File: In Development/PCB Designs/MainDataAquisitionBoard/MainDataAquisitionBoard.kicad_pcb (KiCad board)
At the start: 2 copper layers, 26 parts, among them J1 Motor Driver, J10 3V3, J11 GND, J12 Hall Effect, J13 Hall Effect 2, J14 12V In, J15 Conn_01x08, J16 MotorDriver2, J17 GND In, J2 Conn_01x01, J3 Conn_01x01, J4 1x24, J5 Teensy 3.6L, J6 Teensy 3.6R, J7 1x24, J8 5V, J9 LDS, U1 L7805

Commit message: Finished main DAQ PCB
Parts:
- removed J15: Conn_01x08, Connector_PinHeader_2.54mm:PinHeader_1x08_P2.54mm_Vertical
- removed J16: MotorDriver2, Connector_PinHeader_2.54mm:PinHeader_1x02_P2.54mm_Vertical
- removed J17: GND In, Connector_PinHeader_2.54mm:PinHeader_1x01_P2.54mm_Vertical
- removed U1: L7805, Package_TO_SOT_THT:TO-220-3_Horizontal_TabDown
- J1: value Motor Driver -> Conn_01x08; footprint Connector_PinHeader_2.54mm:PinHeader_1x08_P2.54mm_Vertical -> Connector_PinHeader_2.00mm:PinHeader_1x08_P2.00mm_Vertical
- J10: value 3V3 -> 3v3; footprint Connector_PinHeader_2.54mm:PinHeader_1x05_P2.54mm_Vertical -> Connector_PinHeader_2.54mm:PinHeader_1x04_P2.54mm_Vertical
- J11: value GND -> TopR; footprint Connector_PinHeader_2.54mm:PinHeader_1x05_P2.54mm_Vertical -> CustomKiCADLibrary:PinHeader_1x10_P5.08mm_Vertical
- J12: value Hall Effect -> TopL; footprint Connector_PinHeader_2.54mm:PinHeader_1x04_P2.54mm_Vertical -> CustomKiCADLibrary:PinHeader_1x10_P5.08mm_Vertical
- J13: value Hall Effect 2 -> BottomR; footprint Connector_PinHeader_2.54mm:PinHeader_1x04_P2.54mm_Vertical -> CustomKiCADLibrary:PinHeader_1x10_P5.08mm_Vertical
- J14: value 12V In -> BottomL; footprint Connector_PinHeader_2.54mm:PinHeader_1x01_P2.54mm_Vertical -> CustomKiCADLibrary:PinHeader_1x10_P5.08mm_Vertical
- J2: value Conn_01x01 -> Conn_01x08; footprint Connector_PinHeader_2.54mm:PinHeader_1x01_P2.54mm_Vertical -> Connector_PinHeader_2.00mm:PinHeader_1x08_P2.00mm_Vertical
- J3: value Conn_01x01 -> GND; footprint Connector_PinHeader_2.54mm:PinHeader_1x01_P2.54mm_Vertical -> Connector_PinHeader_2.54mm:PinHeader_1x04_P2.54mm_Vertical
- J8: footprint Connector_PinHeader_2.54mm:PinHeader_1x05_P2.54mm_Vertical -> Connector_PinHeader_2.54mm:PinHeader_1x04_P2.54mm_Vertical
- J9: value LDS -> Conn_01x04; footprint Connector_PinHeader_2.54mm:PinHeader_1x03_P2.54mm_Vertical -> Connector_PinHeader_2.54mm:PinHeader_1x04_P2.54mm_Vertical
- R1, R3, R5, R7: value 5.1k -> 4.7k
- moved J2 139.2 mm to (72.4, 130.8), turned to 180 degrees
- moved J9 108.2 mm to (172.7, 83.8), turned to 90 degrees
- moved R8 102.9 mm to (180.3, 111.8), turned to 90 degrees
- moved J1 100.7 mm to (72.4, 95.2), turned to 180 degrees
- moved R7 100.6 mm to (180.3, 99.1), turned to 90 degrees
- moved R6 99.6 mm to (175.3, 111.8), turned to 90 degrees
- moved R5 96.7 mm to (175.3, 99.1), turned to 90 degrees
- moved J11 88.0 mm to (81.3, 69.8)
- moved J14 80.8 mm to (135.9, 66.0), turned to 90 degrees
- moved J12 70.0 mm to (133.3, 69.8), turned to 90 degrees
- moved J3 56.1 mm to (153.7, 123.2)
- moved J10 27.2 mm to (143.5, 123.2), turned to 0 degrees
- moved J8 27.2 mm to (148.6, 123.2), turned to 0 degrees
- moved J13 20.5 mm to (83.8, 66.0), turned to 90 degrees
- moved R2 19.2 mm to (78.7, 110.5), turned to 90 degrees
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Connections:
- J1 pad 1: Net-(J1-Pad1) -> (no net)
- J1 pad 2: Net-(J1-Pad2) -> (no net)
- J1 pad 5: Net-(J1-Pad5) -> (no net)
- J1 pad 6: Net-(J1-Pad6) -> (no net)
- J1 pad 7: Net-(J1-Pad7) -> (no net)
- J11 pad 1: Net-(J1-Pad1) -> Net-(J11-Pad1)
- J11 pad 2: Net-(J1-Pad1) -> Net-(J11-Pad2)
- J11 pad 3: Net-(J1-Pad1) -> Net-(J11-Pad2)
- J11 pad 4: Net-(J1-Pad1) -> Net-(J11-Pad2)
- J11 pad 5: Net-(J1-Pad1) -> Net-(J11-Pad2)
- J12 pad 2: Net-(J1-Pad1) -> Net-(J10-Pad1)
- J12 pad 3: Net-(J12-Pad3) -> Net-(J10-Pad1)
- J13 pad 1: Net-(J12-Pad1) -> Net-(J13-Pad1)
- J13 pad 2: Net-(J1-Pad1) -> Net-(J13-Pad10)
- J13 pad 3: Net-(J13-Pad3) -> Net-(J13-Pad10)
- J13 pad 4: Net-(J13-Pad4) -> Net-(J13-Pad10)
- J2 pad 1: (no net) -> Net-(J11-Pad2)
- J3 pad 1: (no net) -> Net-(J13-Pad10)
- J4 pad 1: Net-(J1-Pad1) -> Net-(J13-Pad10)
- J4 pad 4: Net-(J1-Pad2) -> Net-(J4-Pad4)
- J4 pad 5: Net-(J1-Pad3) -> Net-(J4-Pad5)
- J4 pad 7: Net-(J4-Pad7) -> Net-(J2-Pad8)
- J4 pad 8: Net-(J4-Pad8) -> Net-(J2-Pad4)
- J5 pad 1: Net-(J1-Pad1) -> Net-(J13-Pad10)
- J5 pad 4: Net-(J1-Pad2) -> Net-(J4-Pad4)
- J5 pad 5: Net-(J1-Pad3) -> Net-(J4-Pad5)
- J5 pad 7: Net-(J4-Pad7) -> Net-(J2-Pad8)
- J5 pad 8: Net-(J4-Pad8) -> Net-(J2-Pad4)
- J6 pad 1: Net-(J12-Pad1) -> Net-(J11-Pad2)
- J6 pad 10: Net-(J6-Pad10) -> Net-(J14-Pad4)
- J6 pad 11: Net-(J13-Pad3) -> Net-(J12-Pad4)
- J6 pad 12: Net-(J13-Pad4) -> Net-(J14-Pad7)
- J6 pad 13: Net-(J6-Pad13) -> Net-(J12-Pad7)
- J6 pad 24: Net-(J6-Pad24) -> Net-(J1-Pad8)
- J6 pad 4: Net-(J6-Pad4) -> Net-(J13-Pad8)
- J6 pad 5: Net-(J6-Pad5) -> Net-(J11-Pad8)
- J6 pad 6: Net-(J6-Pad6) -> Net-(J14-Pad1)
- J6 pad 7: Net-(J12-Pad3) -> Net-(J12-Pad1)
- J6 pad 8: Net-(J12-Pad4) -> Net-(J11-Pad1)
- J6 pad 9: Net-(J6-Pad9) -> Net-(J13-Pad1)
- J7 pad 1: Net-(J12-Pad1) -> Net-(J11-Pad2)
- J7 pad 10: Net-(J6-Pad10) -> Net-(J14-Pad4)
- J7 pad 11: Net-(J13-Pad3) -> Net-(J12-Pad4)
- J7 pad 12: Net-(J13-Pad4) -> Net-(J14-Pad7)
- J7 pad 13: Net-(J6-Pad13) -> Net-(J12-Pad7)
- J7 pad 24: Net-(J6-Pad24) -> Net-(J1-Pad8)
- J7 pad 4: Net-(J6-Pad4) -> Net-(J13-Pad8)
- J7 pad 5: Net-(J6-Pad5) -> Net-(J11-Pad8)
- J7 pad 6: Net-(J6-Pad6) -> Net-(J14-Pad1)
- J7 pad 7: Net-(J12-Pad3) -> Net-(J12-Pad1)
- J7 pad 8: Net-(J12-Pad4) -> Net-(J11-Pad1)
- J7 pad 9: Net-(J6-Pad9) -> Net-(J13-Pad1)
- J8 pad 1: Net-(J12-Pad1) -> Net-(J11-Pad2)
- J8 pad 2: Net-(J12-Pad1) -> Net-(J11-Pad2)
- J8 pad 3: Net-(J12-Pad1) -> Net-(J11-Pad2)
- J8 pad 4: Net-(J12-Pad1) -> Net-(J11-Pad2)
- J9 pad 1: Net-(J12-Pad1) -> Net-(J12-Pad9)
- J9 pad 2: Net-(J6-Pad13) -> Net-(J12-Pad10)
- J9 pad 3: Net-(J1-Pad1) -> Net-(J14-Pad9)
- R1 pad 1: Net-(J12-Pad3) -> Net-(J4-Pad24)
- R1 pad 2: Net-(J12-Pad1) -> Net-(J1-Pad3)
- R2 pad 1: Net-(J12-Pad3) -> Net-(J13-Pad10)
- R2 pad 2: Net-(J1-Pad1) -> Net-(J4-Pad24)
- R3 pad 1: Net-(J12-Pad4) -> Net-(J4-Pad23)
- R3 pad 2: Net-(J12-Pad1) -> Net-(J1-Pad4)
- R4 pad 1: Net-(J12-Pad4) -> Net-(J13-Pad10)
- R4 pad 2: Net-(J1-Pad1) -> Net-(J4-Pad23)
- R5 pad 1: Net-(J13-Pad3) -> Net-(J6-Pad22)
- R5 pad 2: Net-(J12-Pad1) -> Net-(J11-Pad6)
- R6 pad 1: Net-(J13-Pad3) -> Net-(J13-Pad10)
- R6 pad 2: Net-(J1-Pad1) -> Net-(J6-Pad22)
- R7 pad 1: Net-(J13-Pad4) -> Net-(J6-Pad21)
- R7 pad 2: Net-(J12-Pad1) -> Net-(J13-Pad6)
- R8 pad 1: Net-(J13-Pad4) -> Net-(J13-Pad10)
- R8 pad 2: Net-(J1-Pad1) -> Net-(J6-Pad21)
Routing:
- net Net-(J13-Pad10): track 0.00 -> 327.3 mm
- net Net-(J1-Pad1): track 259.8 -> 0.00 mm
- net Net-(J11-Pad2): track 0.00 -> 199.8 mm
- net Net-(J6-Pad21): track 5.08 -> 153.2 mm
- net Net-(J14-Pad7): track 0.00 -> 141.3 mm
- net Net-(J12-Pad1): track 188.9 -> 55.6 mm
- net Net-(J12-Pad7): track 0.00 -> 131.0 mm
- net Net-(J13-Pad1): track 0.00 -> 104.5 mm
- net Net-(J13-Pad6): track 0.00 -> 100.0 mm
- net Net-(J10-Pad1): track 89.7 -> 189.1 mm
- net Net-(J11-Pad1): track 0.00 -> 97.2 mm
- net Net-(J6-Pad22): track 5.08 -> 98.9 mm
- net Net-(J11-Pad6): track 0.00 -> 91.4 mm
- net Net-(J11-Pad8): track 0.00 -> 88.8 mm
- net Net-(J13-Pad8): track 0.00 -> 86.8 mm
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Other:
- board text removed: "3V3"
- board text removed: "5V"
- board text removed: "GND"
- board text removed: "VCC"

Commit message: Finished eCVT protoboard schematic
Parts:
- moved J3 7.62 mm to (161.3, 123.2)
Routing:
- net Net-(J13-Pad10): track 327.3 -> 338.1 mm
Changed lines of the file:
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@@
     (thickness 1.6)
     (drawings 7)
-    (tracks 320)
+    (tracks 323)
     (zones 0)
     (modules 22)
@@
   )
   (module Connector_PinHeader_2.54mm:PinHeader_1x04_P2.54mm_Vertical (layer F.Cu)
-    (at 153.67 123.19)
+    (at 161.29 123.19)
     (descr "Through hole straight pin header, 1x04, 2.54mm pitch, single row")
     (tags "Through hole pin header THT 1x04 2.54mm single row")
@@
   (segment (start 148.59 92.71) (end 148.59 97.79) (width 0.25) (layer F.Cu) (net 39) (status 30))
   (segment (start 148.59 91.61) (end 148.59 92.71) (width 0.25) (layer F.Cu) (net 39) (status 20))
-  (segment (start 153.67 130.81) (end 153.67 123.19) (width 0.25) (layer F.Cu) (net 39) (status 30))
-  (segment (start 153.67 123.19) (end 165.1 111.76) (width 0.25) (layer F.Cu) (net 39) (status 30))
   (segment (start 148.59 98.89) (end 148.59 97.79) (width 0.25) (layer F.Cu) (net 39) (status 20))
   (segment (start 161.46 111.76) (end 148.59 98.89) (width 0.25) (layer F.Cu) (net 39))
@@
   (segment (start 106.68 63.5) (end 111.76 63.5) (width 0.25) (layer F.Cu) (net 39))
   (segment (start 78.93 133.35) (end 72.39 126.81) (width 0.25) (layer F.Cu) (net 39))
-  (segment (start 153.67 130.81) (end 151.13 133.35) (width 0.25) (layer F.Cu) (net 39))
   (segment (start 151.13 133.35) (end 78.93 133.35) (width 0.25) (layer F.Cu) (net 39))
   (segment (start 78.74 120.46) (end 78.74 110.49) (width 0.25) (layer F.Cu) (net 39))
   (segment (start 72.39 126.81) (end 78.74 120.46) (width 0.25) (layer F.Cu) (net 39))
   (segment (start 78.74 110.49) (end 83.82 110.49) (width 0.25) (layer F.Cu) (net 39))
+  (segment (start 161.29 122.09) (end 161.29 123.19) (width 0.25) (layer F.Cu) (net 39))
+  (segment (start 171.62 111.76) (end 161.29 122.09) (width 0.25) (layer F.Cu) (net 39))
+  (segment (start 175.26 111.76) (end 171.62 111.76) (width 0.25) (layer F.Cu) (net 39))
+  (segment (start 161.29 123.19) (end 161.29 130.81) (width 0.25) (layer F.Cu) (net 39))
+  (segment (start 161.29 130.81) (end 158.75 133.35) (width 0.25) (layer F.Cu) (net 39))
+  (segment (start 158.75 133.35) (end 151.13 133.35) (width 0.25) (layer F.Cu) (net 39))
   (segment (start 130.81 92.71) (end 130.81 97.79) (width 0.25) (layer F.Cu) (net 40) (status 30))
   (segment (start 73.064999 124.135001) (end 76.524999 124.135001) (width 0.25) (layer B.Cu) (net 40))

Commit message: Finished Main DAQ PCB rev 2
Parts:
- removed R1, R3: 4.7k, Resistor_THT:R_Axial_DIN0207_L6.3mm_D2.5mm_P7.62mm_Horizontal
- removed R2, R4: 8.2k, Resistor_THT:R_Axial_DIN0207_L6.3mm_D2.5mm_P7.62mm_Horizontal
- added J15: RTC, Connector_PinHeader_2.54mm:PinHeader_1x08_P2.54mm_Vertical, F.Cu at (109.2, 113.0)
- moved J5 10.2 mm to (148.6, 87.6)
- moved J4 10.2 mm to (148.6, 82.5)
- moved J6 10.2 mm to (148.6, 102.9)
- moved J7 10.2 mm to (148.6, 108.0)
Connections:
- J4 pad 23: Net-(J4-Pad23) -> Net-(J1-Pad4)
- J4 pad 24: Net-(J4-Pad24) -> Net-(J1-Pad3)
- J5 pad 23: Net-(J4-Pad23) -> Net-(J1-Pad4)
- J5 pad 24: Net-(J4-Pad24) -> Net-(J1-Pad3)
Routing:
- net Net-(J10-Pad1): track 189.1 -> 248.9 mm
- net Net-(J6-Pad21): track 153.2 -> 187.2 mm
- net Net-(J13-Pad10): track 338.1 -> 369.4 mm
- net Net-(J11-Pad1): track 97.2 -> 125.5 mm
- net Net-(J11-Pad2): track 199.8 -> 226.1 mm
- net Net-(J4-Pad24): track 21.9 -> 0.00 mm
- net Net-(J13-Pad1): track 104.5 -> 125.4 mm
- net Net-(J4-Pad23): track 19.4 -> 0.00 mm
- net Net-(J1-Pad3): track 6.43 -> 24.4 mm
- net Net-(J1-Pad4): track 12.3 -> 28.2 mm
- net Net-(J14-Pad1): track 59.4 -> 49.3 mm
- net Net-(J13-Pad8): track 86.8 -> 76.7 mm
- net Net-(J12-Pad1): track 55.6 -> 45.5 mm
- net Net-(J11-Pad8): track 88.8 -> 78.6 mm
- net Net-(J14-Pad4): track 65.1 -> 54.9 mm
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
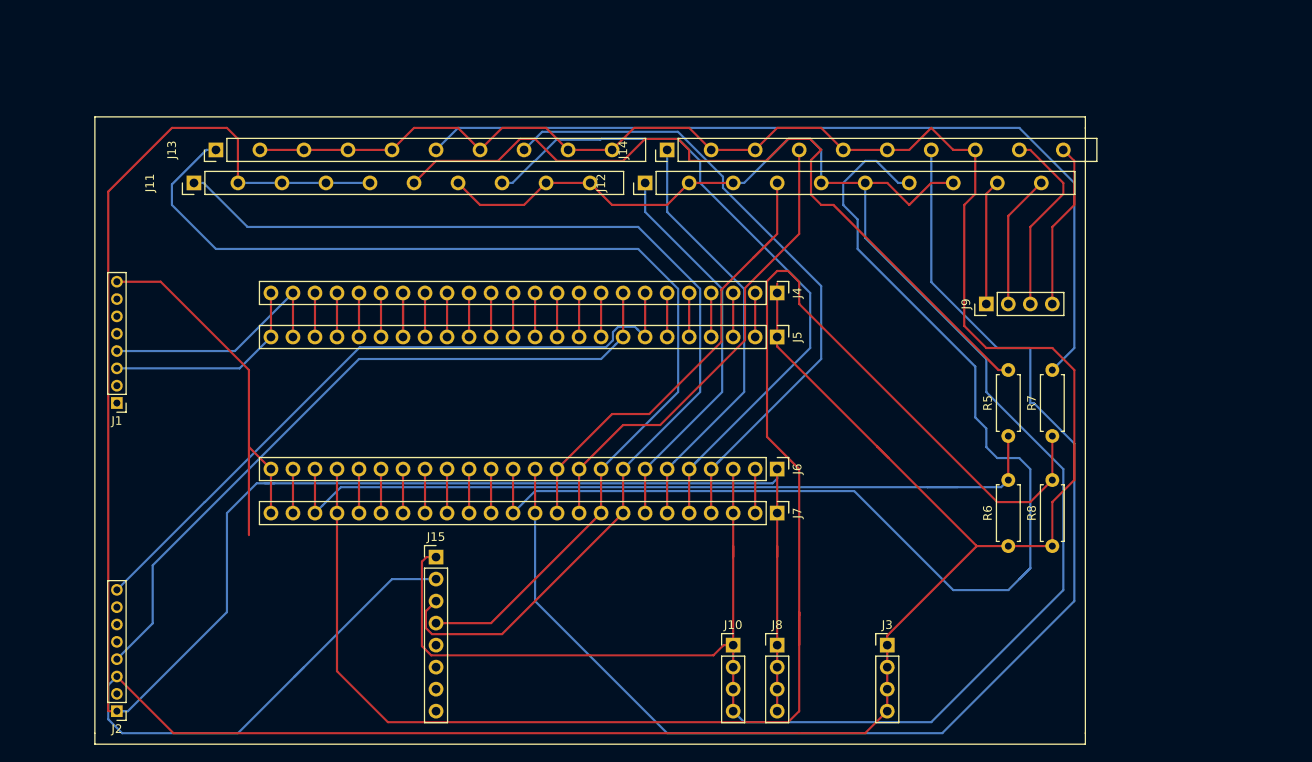
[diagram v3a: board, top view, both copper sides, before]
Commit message: Finished Main DAQ PCB and eCVT controller PCB for design review
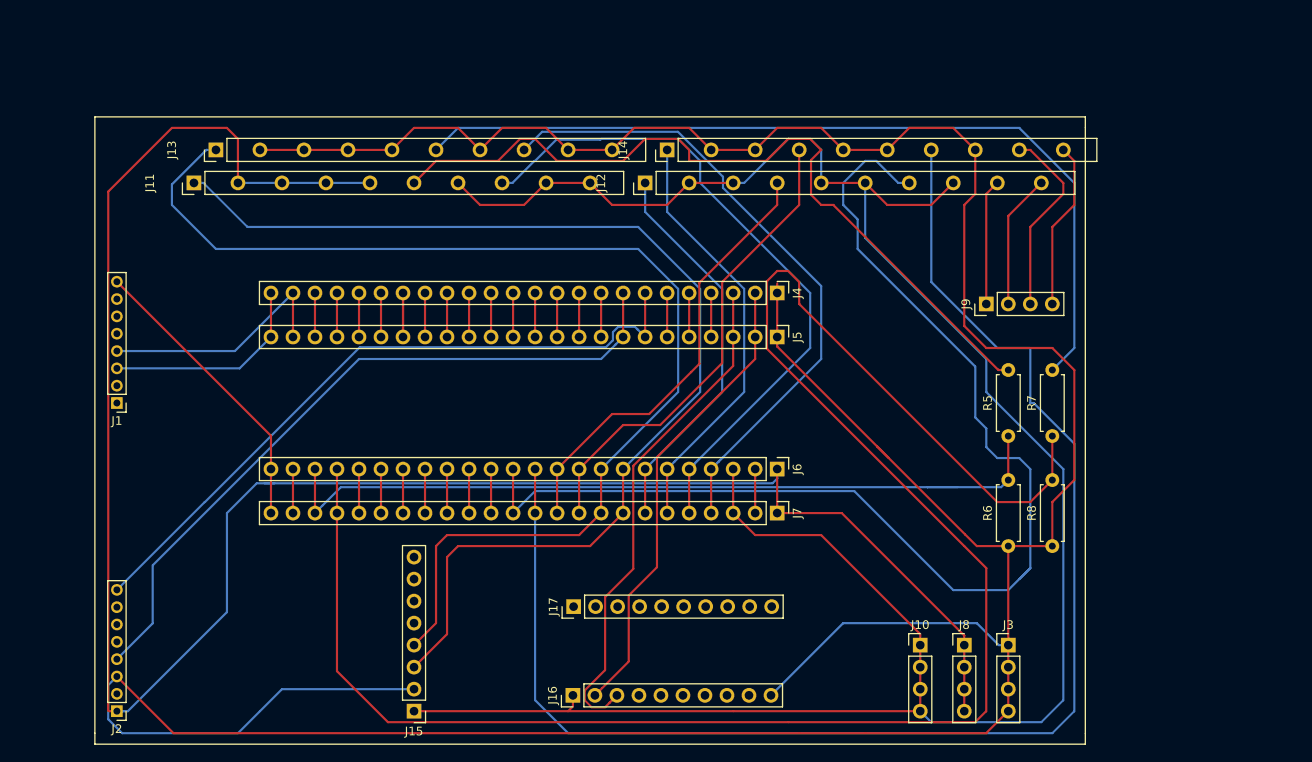
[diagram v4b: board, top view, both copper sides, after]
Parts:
- added J16: XbeeL, Connector_PinHeader_2.54mm:PinHeader_1x10_P2.54mm_Vertical, F.Cu at (125.0, 129.0)
- added J17: XbeeR, Connector_PinHeader_2.54mm:PinHeader_1x10_P2.54mm_Vertical, F.Cu at (125.1, 118.7)
- moved J10 21.6 mm to (165.1, 123.2)
- moved J8 21.6 mm to (170.2, 123.2)
- moved J15 18.0 mm to (106.7, 130.8), turned to 180 degrees
- moved J3 14.0 mm to (175.3, 123.2)
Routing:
- net Net-(J16-Pad3): track 5.08 -> 58.7 mm
- net Net-(J16-Pad2): track 5.08 -> 54.1 mm
- net Net-(J13-Pad10): track 369.4 -> 401.6 mm
- net Net-(J6-Pad21): track 187.2 -> 213.4 mm
- net Net-(J14-Pad7): track 151.5 -> 165.6 mm
- net Net-(J1-Pad8): track 47.2 -> 34.1 mm
- net Net-(J11-Pad2): track 226.1 -> 238.1 mm
- net Net-(J10-Pad1): track 248.9 -> 259.0 mm
- net Net-(J13-Pad1): track 125.4 -> 134.2 mm
- net Net-(J11-Pad1): track 125.5 -> 129.7 mm
- net Net-(J12-Pad4): track 54.4 -> 51.1 mm

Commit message: Finished DAQ board and ready for initial production
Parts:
- added J18: Conn_02x03_Counter_Clockwise, Connector_PinHeader_2.54mm:PinHeader_2x03_P2.54mm_Vertical, F.Cu at (157.5, 102.9)
- added J19: Power in, CustomKiCADLibrary:PinHeader_1x02_P5.08mm_Vertical, F.Cu at (176.5, 129.5)
- moved J17 16.2 mm to (135.9, 130.8), turned to 270 degrees
- moved J16 15.4 mm to (135.9, 118.1), turned to 270 degrees
- moved J14 13.1 mm to (129.5, 54.6)
- moved J13 12.5 mm to (78.7, 54.6)
- moved J15 7.62 mm to (99.1, 130.8)
- moved J1 6.35 mm to (66.0, 95.2)
- moved J10 6.35 mm to (158.8, 123.2)
- moved J2 6.35 mm to (66.0, 130.8)
- moved J3 6.35 mm to (168.9, 123.2)
- moved J8 6.35 mm to (163.8, 123.2)
- moved J12 1.27 mm to (132.1, 69.8)
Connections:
- J1 pad 1: (no net) -> Net-(J1-Pad1)
- J13 pad 10: Net-(J13-Pad10) -> Net-(J1-Pad1)
- J13 pad 2: Net-(J13-Pad10) -> Net-(J1-Pad1)
- J13 pad 3: Net-(J13-Pad10) -> Net-(J1-Pad1)
- J13 pad 4: Net-(J13-Pad10) -> Net-(J1-Pad1)
- J13 pad 5: Net-(J13-Pad10) -> Net-(J1-Pad1)
- J13 pad 7: Net-(J13-Pad10) -> Net-(J1-Pad1)
- J13 pad 9: Net-(J13-Pad10) -> Net-(J1-Pad1)
- J14 pad 2: Net-(J13-Pad10) -> Net-(J1-Pad1)
- J14 pad 3: Net-(J13-Pad10) -> Net-(J1-Pad1)
- J14 pad 5: Net-(J13-Pad10) -> Net-(J1-Pad1)
- J14 pad 6: Net-(J13-Pad10) -> Net-(J1-Pad1)
- J14 pad 8: Net-(J13-Pad10) -> Net-(J1-Pad1)
- J15 pad 2: Net-(J13-Pad10) -> Net-(J1-Pad1)
- J16 pad 10: Net-(J13-Pad10) -> Net-(J1-Pad1)
- J2 pad 1: Net-(J11-Pad2) -> Net-(J2-Pad1)
- J2 pad 3: Net-(J13-Pad10) -> Net-(J2-Pad3)
- J3 pad 1: Net-(J13-Pad10) -> Net-(J1-Pad1)
- J3 pad 2: Net-(J13-Pad10) -> Net-(J1-Pad1)
- J3 pad 3: Net-(J13-Pad10) -> Net-(J1-Pad1)
- J3 pad 4: Net-(J13-Pad10) -> Net-(J1-Pad1)
- J4 pad 1: Net-(J13-Pad10) -> Net-(J1-Pad1)
- J4 pad 11: Net-(J4-Pad11) -> Net-(J2-Pad3)
- J4 pad 12: Net-(J4-Pad12) -> Net-(J2-Pad1)
- J5 pad 1: Net-(J13-Pad10) -> Net-(J1-Pad1)
- J5 pad 11: Net-(J4-Pad11) -> Net-(J2-Pad3)
- J5 pad 12: Net-(J4-Pad12) -> Net-(J2-Pad1)
- J6 pad 1: Net-(J11-Pad2) -> Net-(J18-Pad3)
- J7 pad 1: Net-(J11-Pad2) -> Net-(J18-Pad3)
- R6 pad 1: Net-(J13-Pad10) -> Net-(J1-Pad1)
- R8 pad 1: Net-(J13-Pad10) -> Net-(J1-Pad1)
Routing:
- net Net-(J13-Pad10): track 401.6 -> 0.00 mm
- net Net-(J1-Pad1): track 0.00 -> 363.0 mm
- net Net-(J2-Pad1): track 0.00 -> 90.5 mm
- net Net-(J2-Pad3): track 0.00 -> 86.6 mm
- net Net-(J6-Pad21): track 213.4 -> 147.9 mm
- net Net-(J10-Pad1): track 259.0 -> 294.9 mm
- net Net-(J14-Pad7): track 165.6 -> 201.0 mm
- net Net-(J11-Pad6): track 91.4 -> 110.3 mm
- net Net-(J13-Pad1): track 134.2 -> 152.9 mm
- net Net-(J11-Pad8): track 78.6 -> 96.7 mm
- net Net-(J16-Pad3): track 58.7 -> 40.8 mm
- net Net-(J13-Pad8): track 76.7 -> 93.2 mm
- net Net-(J18-Pad3): track 0.00 -> 15.0 mm
- net Net-(J14-Pad10): track 19.4 -> 33.4 mm
- net Net-(J14-Pad1): track 49.3 -> 63.3 mm
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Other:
- board text added: "+"
- board text added: "-"
- board text added: "3V3"
- board text added: "4.7k"
- board text added: "5V"
- board text added: "8.2k"
- board text added: "GND"
- board text added: "ON"
- board text added: "Programming Mode"

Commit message: Fixed edge cuts on DAQ PCB
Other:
- board outline added: 120.7 x 83.8 mm
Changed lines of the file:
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@@
   (general
     (thickness 1.6)
-    (drawings 21)
+    (drawings 15)
     (tracks 392)
     (zones 0)
@@
     (42 Eco1.User user hide)
     (43 Eco2.User user hide)
-    (44 Edge.Cuts user hide)
+    (44 Edge.Cuts user)
     (45 Margin user)
     (46 B.CrtYd user hide)
@@
       (net 53 "Net-(J1-Pad1)"))
   )
+  (gr_line (start 184.15 50.8) (end 184.15 134.62) (layer Edge.Cuts) (width 0.12))
+  (gr_line (start 63.5 50.8) (end 184.15 50.8) (layer Edge.Cuts) (width 0.12))
+  (gr_line (start 63.5 134.62) (end 63.5 50.8) (layer Edge.Cuts) (width 0.12))
+  (gr_line (start 184.15 134.62) (end 63.5 134.62) (layer Edge.Cuts) (width 0.12))
   (gr_text "Programming\nMode" (at 159.385 111.76) (layer F.SilkS)
     (effects (font (size 1 1) (thickness 0.15)))
@@
     (effects (font (size 1 1) (thickness 0.15)))
   )
-  (gr_line (start 184.15 50.8) (end 184.15 62.23) (layer F.SilkS) (width 0.12))
-  (gr_line (start 63.5 50.8) (end 184.15 50.8) (layer F.SilkS) (width 0.12))
-  (gr_line (start 63.5 62.23) (end 63.5 50.8) (layer F.SilkS) (width 0.12))
-  (gr_line (start 63.5 134.62) (end 69.85 134.62) (layer F.SilkS) (width 0.12))
-  (gr_line (start 63.5 62.23) (end 63.5 134.62) (layer F.SilkS) (width 0.12))
-  (gr_line (start 184.15 134.62) (end 184.15 133.35) (layer F.SilkS) (width 0.12))
-  (gr_line (start 69.85 134.62) (end 184.15 134.62) (layer F.SilkS) (width 0.12))
-  (gr_line (start 69.85 133.35) (end 69.85 134.62) (layer F.SilkS) (width 0.12))
-  (gr_line (start 184.15 63.5) (end 184.15 62.23) (layer F.SilkS) (width 0.12))
-  (gr_line (start 184.15 133.35) (end 184.15 63.5) (layer F.SilkS) (width 0.12))
   (segment (start 90.17 82.55) (end 90.17 87.63) (width 0.25) (layer F.Cu) (net 1) (status 30))
   (segment (start 86.55 91.25) (end 90.17 87.63) (width 0.25) (layer B.Cu) (net 1) (status 20))
@@
   (segment (start 97.79 102.87) (end 97.79 107.95) (width 0.25) (layer F.Cu) (net 27) (status 30))
   (segment (start 180.34 104.14) (end 180.34 99.06) (width 0.25) (layer F.Cu) (net 27) (status 30))
+  (segment (start 95.25 110.49) (end 97.79 107.95) (width 0.25) (layer F.Cu) (net 27))
   (segment (start 180.34 104.14) (end 181.61 105.41) (width 0.25) (layer F.Cu) (net 27))
   (segment (start 181.61 105.41) (end 181.61 129.54) (width 0.25) (layer F.Cu) (net 27))
   (segment (start 181.61 129.54) (end 179.07 132.08) (width 0.25) (layer F.Cu) (net 27))
-  (segment (start 95.25 110.49) (end 97.79 107.95) (width 0.25) (layer F.Cu) (net 27))
-  (segment (start 95.25 130.81) (end 96.52 132.08) (width 0.25) (layer F.Cu) (net 27))
-  (segment (start 95.25 110.49) (end 95.25 130.81) (width 0.25) (layer F.Cu) (net 27))
+  (segment (start 96.52 132.08) (end 95.25 130.81) (width 0.25) (layer F.Cu) (net 27))
   (segment (start 179.07 132.08) (end 96.52 132.08) (width 0.25) (layer F.Cu) (net 27))
+  (segment (start 95.25 130.81) (end 95.25 110.49) (width 0.25) (layer F.Cu) (net 27))
   (segment (start 95.25 102.87) (end 95.25 107.95) (width 0.25) (layer F.Cu) (net 28) (status 30))
   (segment (start 175.26 104.14) (end 175.26 99.06) (width 0.25) (layer F.Cu) (net 28) (status 30))
